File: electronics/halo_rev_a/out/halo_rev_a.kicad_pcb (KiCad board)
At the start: 4 copper layers, 25.6 x 26 mm, 51 parts, among them J1 Tag-Connect_TC2030-IDC-NL_2x0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, U1 QFN-48-1EP_6x6mm_P0.4mm_EP4.4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, U2 LGA-12_2x2mm_P0.5mm, U3 Winbond_USON-8-1EP_3x2mm_P0.5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, X1 Crystal_SMD_3215-2Pin_3.2x1.5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, X2 Crystal_SMD_2016-4Pin_2.0x1.6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

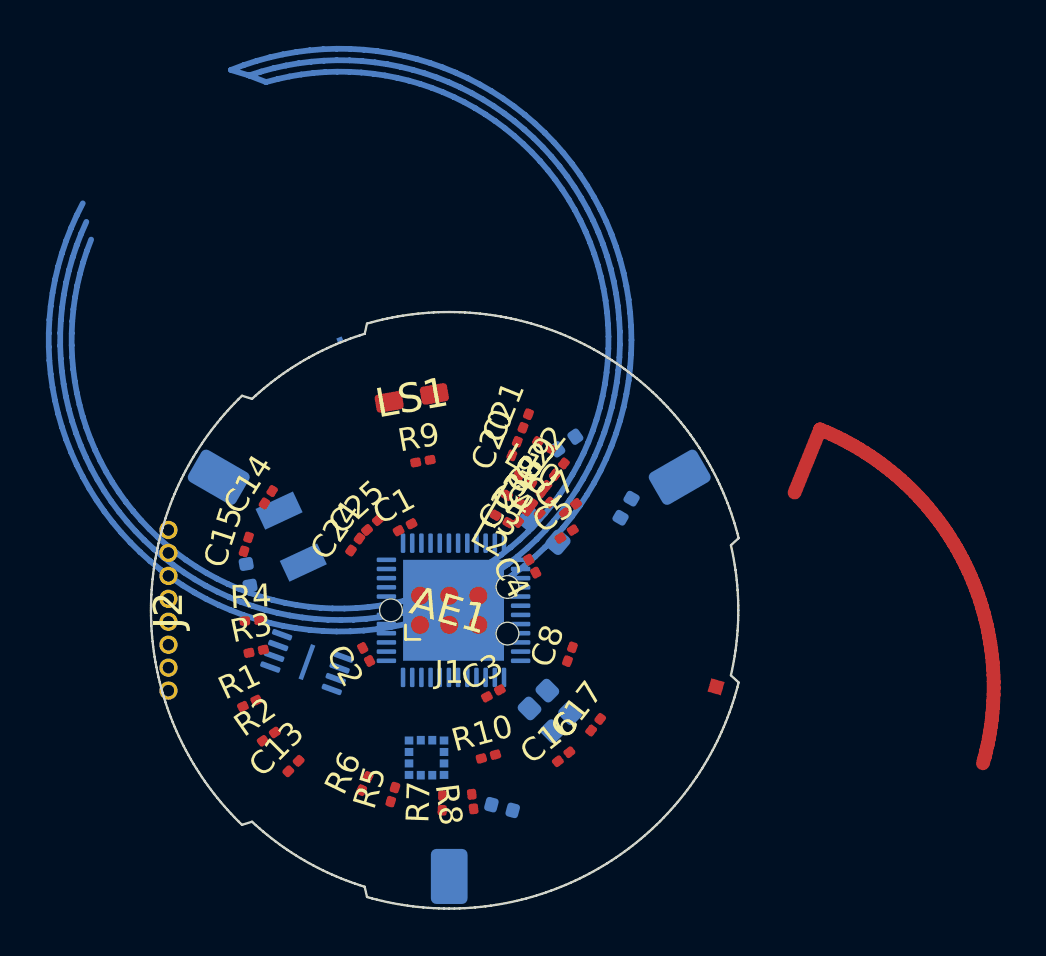
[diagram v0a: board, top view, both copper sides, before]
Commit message: electronics (lane B1): board DRC 449 -> 20 violations, with the reasons
Every fix below is a measured cause, not a tightened tolerance. Nothing was
excluded, silenced or loosened to make a count fall.

THE CONTACT LANDS WERE POINTING THE WRONG WAY, and it cost 1.2 mm of copper
in the wrong direction. A pad at position angle t has its radius along
(cos t, -sin t) in KiCad's Y-down frame, and a pad rotated by phi has its
LONG axis along (cos phi, -sin phi) - so authoring phi = t pointed each
2.40 mm contact strip RADIALLY. The lands spanned R10.4 to R12.8 instead of
R11.0 to R12.2: into the NFC winding on one side, and to within 0.35 mm of
the routed edge on the other. Found from the DRC's own coordinates rather
than by eye. Tangential is phi = t + 90.

THE RULE THAT FIRED WAS NOT THE RULE THE REPORT NAMED. The DRC said 'board
setup constraints edge clearance 0.5000 mm; actual 0.3478' - KiCad's default
- while this board's own report cited JLCPCB's process. Board.rules() writes
clearance, track, via and hole rules and does NOT write board-edge or solder
mask constraints, so KiCad silently used its own. Both are now written
explicitly with the fab number each comes from, and verify_rules() reads the
project file BACK and prints what the DRC will actually apply: 3 of 3
written and read back.

ETCHED COPPER IS TRACKS NOW, after two constructs that each produced a board
that looked right and failed its own checks. A custom pad with open gr_line
primitives gets CLOSED AND FILLED by KiCad, turning a 3-turn coil into a
solid 25 mm disc. Footprint graphics on a copper layer stroke correctly but
carry no net, so the DRC demanded clearance between the antenna and its own
feed pad. A closed-ribbon custom pad is refused by name: 'Padstack is not
valid (custom pad shape must resolve to a single polygon)'. A track is
arbitrary in shape, on a net, and plots as copper. The NFC coil uses KiCad's
own NetTie-2_SMD_Pad0.5mm mid-winding, because a coil is a short at DC and a
net tie is ho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
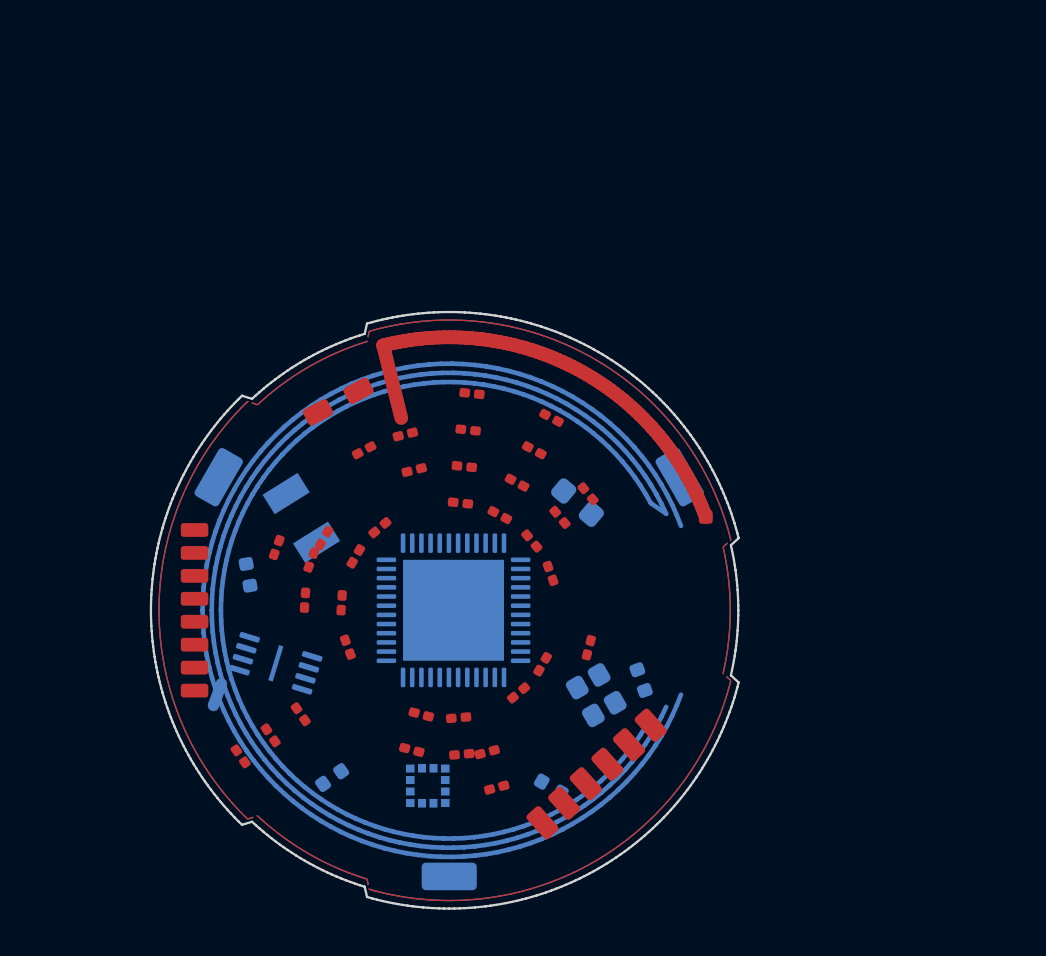
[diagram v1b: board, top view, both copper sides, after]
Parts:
- AE1: footprint HALO_ANT_2G4_MONOPOLE -> HALO_ANT_2G4_FEED
- AE2: value (none) -> NetTie-2_SMD_Pad0.5mm; footprint HALO_NFC_COIL_3T -> NetTie-2_SMD_Pad0.5mm
- J1: value Tag-Connect_TC2030-IDC-NL_2x03_P1.27mm_Vertical -> (none); footprint Tag-Connect_TC2030-IDC-NL_2x03_P1.27mm_Vertical -> HALO_SWD_PADS_1x06_P1.27
- J2: footprint HALO_CASTELLATED_1x08_P1.00 -> HALO_UWB_LANDS_1x08_P1.00
- moved C10 15.0 mm to (17.4, 20.7), turned to -30 degrees
- moved AE1 11.9 mm to (24.2, 8.93), turned to 0 degrees
- moved AE2 10.8 mm to (2.90, 16.7), turned to 70 degrees
- moved J1 9.60 mm to (19.4, 20.1), turned to 42 degrees
- moved C12 7.52 mm to (7.90, 20.3), turned to 35 degrees
- moved C9 7.52 mm to (21.4, 16.0), turned to -70 degrees
- moved R10 6.46 mm to (19.1, 14.6), turned to -105 degrees
- moved C21 5.28 mm to (11.1, 5.33), turned to 14 degrees
- moved C17 5.11 mm to (15.1, 20.7), turned to -165 degrees
- moved C22 5.04 mm to (14.0, 3.55), turned to -6 degrees
- moved C20 4.47 mm to (11.5, 6.89), turned to 14 degrees
- moved R3 4.28 mm to (8.31, 12.7), turned to 86 degrees
- moved C19 4.22 mm to (13.8, 5.14), turned to -6 degrees
- moved R7 3.78 mm to (13.4, 17.7), turned to -175 degrees
- moved R5 3.71 mm to (11.8, 17.5), turned to 165 degrees
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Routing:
- net NFC2: track 0.00 -> 110.0 mm
- net NFC1: track 0.00 -> 60.0 mm
- net ANT_FEED: track 0.00 -> 20.7 mm

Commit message: sim (lane B1): our own rail under the nRF54L10's own transmit pulse - PASS
ce-spice ships cr2032_pulse_load and it models a DIFFERENT BOARD: 8 mA from
an nRF52832 behind 100 uF. Leif asked for our board simulated, so this is
halo rev A's rail with halo rev A's numbers.

  load       8.0 mA -> 3.7 mA   nRF54L10 datasheet Table 86, ITX,0dBm
  reservoir  100 uF -> 40 uF    4 x 10 uF 0402, because 0805 does not fit
  sleep      2.0 uA -> 2.4 uA   Table 86 ION_IDLE4, 192 kB retained

Those move the droop in opposite directions, so which wins was a question
with a number as its answer. Six circuits, VERDICT PASS.

  worst case, 2.0 V cell at 140 ohm: droop 84.7 mV against a 400 mV limit,
  rail bottoms at 1.915 V against the nRF54L's 1.7 V minimum, and the cell
  never sees more than 0.61 mA of the 3.7 mA edge - the bulk carries the
  rest, which is what it is for. Battery life 64.5 months derated.

  the control, same cell with the bulk REMOVED: 517.7 mV of droop and the
  rail collapses to 1.482 V. It asserts its own collapse and PASSES by
  failing electrically, which is the evidence that C9-C12 are load-bearing
  rather than decoration. A study whose every assert is written to pass has
  not been tested.

THE FIVE-REMOVALS RESET IS NOW MEASURED, not asserted. SPEC.md section 3
says the AirTag's bulk is what keeps it alive for seconds after the cell is
pulled. Rev A's schematic D-5 detects the removal on a sense-only contact;
this measures whether the rail actually outlives it. Pulling the cell at
t = 0.5 s, 40 uF holds above 1.7 V for 4.998 s. Apple's 500 uF would give
62.47 s - the price of D-4's re-sizing, as a number rather than a worry.

AN ASSERT WAS REMOVED, AND NOT BECAUSE IT FAILED. The first version asserted
the rail above 1.7 V ten seconds after removal, and it failed at 1.400 V.
Ten seconds came from nowhere: no document requires it and it was written
here as prose, not a requirement. The right response was neither to loosen
it nor to keep it. The real requ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
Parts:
- C14, C15, C16, C17: moved to B.Cu
- moved C14 5.98 mm to (9.23, 5.27), turned to -26 degrees
- moved C15 4.75 mm to (7.82, 6.13), turned to -37 degrees
- moved C16 4.00 mm to (18.6, 19.5), turned to -41 degrees
- moved AE2 3.68 mm to (2.68, 13.0), turned to 180 degrees
- moved C17 2.52 mm to (17.6, 20.3), turned to -32 degrees
- moved C9 1.86 mm to (21.4, 14.2), turned to -82 degrees
- moved C10 0.73 mm to (16.7, 20.6), turned to -26 degrees
- moved X1 0.65 mm to (7.20, 9.09), turned to -56 degrees
- moved U3 0.60 mm to (6.02, 15.1)
- moved C11 0.50 mm to (4.58, 11.8), turned to -82 degrees
- moved C12 0.40 mm to (8.12, 20.0)
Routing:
- net NFC1: track 60.0 -> 0.00 mm
- net NFC2: track 110.0 -> 127.6 mm

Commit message: electronics (lane B1): flash deleted as out-of-spec, test access designed in, antenna re-sized from a measurement
THE FLASH WAS A REAL DEFECT AND IT IS GONE. U3 was a GD25LQ32EEIGR sitting
on VDD, which on this board is a raw CR2032 with no regulator anywhere. That
part's supply range is 1.65 to 2.0 V and a fresh coin cell is 3.0 V, so it
was out of specification from the first second - the kind of fault that
half-works on a bench and fails in a field. Caught by the production test
lane reading the sheet.

Fitting a regulator was the other way out and it is what the real AirTag
does (a TPS62746 buck plus an FPF2487 load switch, SPEC.md section 3). It
would have cost a part, an inductor, a rail, a test and board area this disc
does not have, and bought nothing: the SoC, the accelerometer and the bender
all span the whole cell curve unaided. research/05 section 3.7 and
spec/bom-candidates.json already recommended omitting the flash, and the
firmware lane has since measured the whole firmware at 13,164 bytes - 1.27
percent of the nRF54L10's own 1 MB. So it is deleted: a part, a rail
problem, two pull-ups, nine joints and a production test. If revision B ever
wants external firmware staging the part is a wide-range low-power NOR such
as the Macronix MX25R, specified 1.65 to 3.6 V, which is the range a coin
cell actually presents.

TEST ACCESS IS DESIGNED IN. Eleven probe lands, and VDD and GND each get a
FORCE and a SENSE pad rather than one pad each - sleep current here is
single-digit microamps and a two-wire reading measures the probe, while two
probes in one battery pad is a two-wire measurement wearing a four-wire
name. Plus both piezo nets, which otherwise terminate on the shell; the
cell-removal sense node; the I2C bus; both NFC pins; and two fiducials.
IPC-A-610 CLASS 2 is recorded on the sheet, because the AOI recipe is built
from it and nobody had chosen one.

THEY ARE PLACED BY SEARCH, NOT BY HAND. Hand-placing thirteen things into a
full board produced eight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
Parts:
- removed R3, R4: R_0201_0603Metric, R_0201_0603Metric
- removed U3: Winbond_USON-8-1EP_3x2mm_P0.5mm_EP0.2x1.6mm, Winbond_USON-8-1EP_3x2mm_P0.5mm_EP0.2x1.6mm
- added FID1: Fiducial_0.5mm_Mask1mm, Fiducial_0.5mm_Mask1mm, F.Cu at (9.72, 22.0)
- added FID2: Fiducial_0.5mm_Mask1mm, Fiducial_0.5mm_Mask1mm, F.Cu at (9.25, 16.9)
- added TP1: , HALO_TP_D0.8, F.Cu at (16.4, 13.2)
- added TP10: , HALO_TP_D0.8, F.Cu at (20.8, 13.5)
- added TP11: , HALO_TP_D0.8, F.Cu at (12.2, 21.0)
- added TP2: , HALO_TP_D0.8, F.Cu at (9.61, 12.7)
- added TP3: , HALO_TP_D0.8, F.Cu at (7.61, 12.6)
- added TP4: , HALO_TP_D0.8, F.Cu at (19.2, 12.6)
- added TP5: , HALO_TP_D0.8, F.Cu at (12.1, 9.72)
- added TP6: , HALO_TP_D0.8, F.Cu at (19.3, 10.6)
- added TP7: , HALO_TP_D0.8, F.Cu at (6.61, 15.3)
- added TP8: , HALO_TP_D0.8, F.Cu at (8.23, 7.88)
- added TP9: , HALO_TP_D0.8, F.Cu at (9.08, 19.0)
- moved C10 1.48 mm to (15.3, 21.2), turned to -16 degrees
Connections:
- U1 pad 16: FLASH_CS -> unconnected-(U1-P2.05/CS-Pad16)
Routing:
- net ANT_FEED: track 20.7 -> 24.5 mm

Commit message: fab (lane B1): the factory package - gerbers with geometry, a BOM with order codes, ERC 0/0
ERC PASS, 0 errors AND 0 WARNINGS. The 13 warnings before this were one
cause: this machine has no global KiCad footprint table, because KiCad has
never been opened interactively here, so without a project table ERC cannot
resolve a footprint and reports one warning per part. The project now writes
its own listing all 155 KiCad libraries plus halo's, which also makes the
handoff self-contained. It is written at the END of the pipeline because
bin/sch build writes its own 8-library version over anything earlier - an
attempt to write it from the schematic was silently discarded.

THE GERBERS ARE VERIFIED, NOT ASSUMED. The factory lane warned that gerber
export had been failing silently for everyone - a flag that does not exist
in KiCad 10 while the pipeline reported success - so these were opened
rather than trusted: F_Cu carries 3265 draw commands and Edge_Cuts 720. 13
files in the zip, layer check PASS against JLCPCB's published naming table,
plus two Excellon drills and a drill map.

THE BOM CARRIES ORDER CODES NOW, and it did not an hour ago. Two silent
failures stacked. First, the field was named 'LCSC' and ce-fab looks for
'LCSC Part #' and five other spellings - a plain 'LCSC' is in none of them.
Second, and worse, Board.place() puts a land pattern down without the part's
value or its fields, because those live on the schematic; fab jlc reads the
.kicad_pcb, so every order code was on the sheet and NOT ONE reached the
bill of materials. The board now imports the schematic and copies 61 values
and 324 fields across. 24 BOM lines with real codes; the six parts with no
code are AE1 and AE2, which are etched copper, and C14-C17, which are not
fitted. Those are correct answers, not gaps.

THE RULE THAT FIRES IS NOW THE RULE THE REPORT NAMES - the other trap the
factory lane flagged. The DRC had been running against KiCad's 0.5 mm
default board-edge clearance while this board'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
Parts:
- AE1: value (none) -> 2G4 PCB antenna
- AE2: value NetTie-2_SMD_Pad0.5mm -> NFC coil 13.56MHz
- BT1: value (none) -> CR2032
- C1, C2, C3, C4: value C_0201_0603Metric -> 100nF
- C10, C11, C12, C9: value C_0402_1005Metric -> 10uF
- C13: value C_0201_0603Metric -> 100pF
- C14, C15, C16, C17: value C_0201_0603Metric -> DNP
- C18: value C_0201_0603Metric -> 1.5pF
- C19: value C_0201_0603Metric -> 2.0pF
- C20, C21: value C_0201_0603Metric -> 0.5pF
- C22: value C_0201_0603Metric -> 0.3pF
- C23: value C_0201_0603Metric -> 3.9pF
- C24, C25: value C_0201_0603Metric -> 1.1nF
- C5, C8: value C_0201_0603Metric -> 2.2uF
- C6: value C_0201_0603Metric -> 10nF
- C7: value C_0201_0603Metric -> 2.2nF
- FID1, FID2: value Fiducial_0.5mm_Mask1mm -> FIDUCIAL
- J1: value (none) -> TC2030
- J2: value (none) -> UWB stub
- L1: value L_0603_1608Metric -> 4.7uH
- L10: value L_0201_0603Metric -> 0R
- L2: value L_0201_0603Metric -> 2.7nH
- L3, L4: value L_0201_0603Metric -> 3.5nH
- LS1: value (none) -> 7BB-20-3
- R1, R2: value R_0201_0603Metric -> 4.7M
- R10, R5, R6, R7, R8: value R_0201_0603Metric -> 10k
- R9: value R_0201_0603Metric -> 100R
- TP1, TP10, TP11, TP2, TP3, TP4, TP5, TP6, TP7, TP8, TP9: value (none) -> TP
- U1: value QFN-48-1EP_6x6mm_P0.4mm_EP4.4x4.4mm -> nRF54L10-QFAA-R7
- U2: value LGA-12_2x2mm_P0.5mm -> LIS2DW12TR
- X1: value Crystal_SMD_3215-2Pin_3.2x1.5mm -> 32.768kHz
- X2: value Crystal_SMD_2016-4Pin_2.0x1.6mm -> 32MHz
